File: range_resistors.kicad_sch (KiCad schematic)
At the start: 8 parts, among them U10 74HC4051

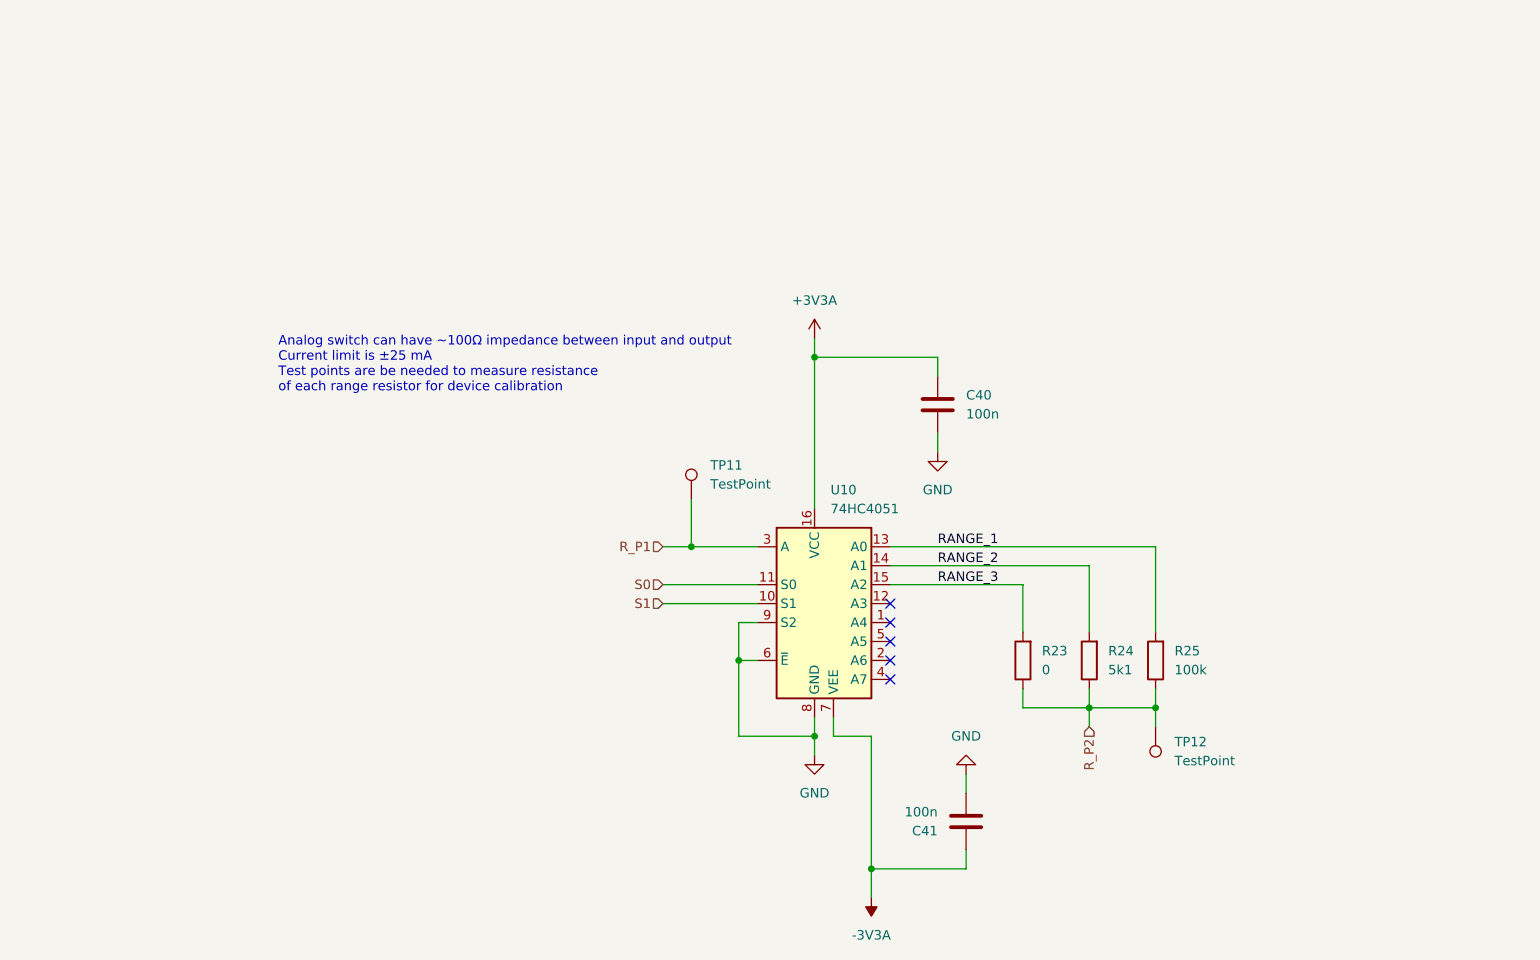
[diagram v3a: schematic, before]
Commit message: Changed range resistor selector design
Changed range resistor selector from an analog mux
to a MOSFET BPS design. This should improve on resistance, linearity,
and temperature stability for the range resistors.
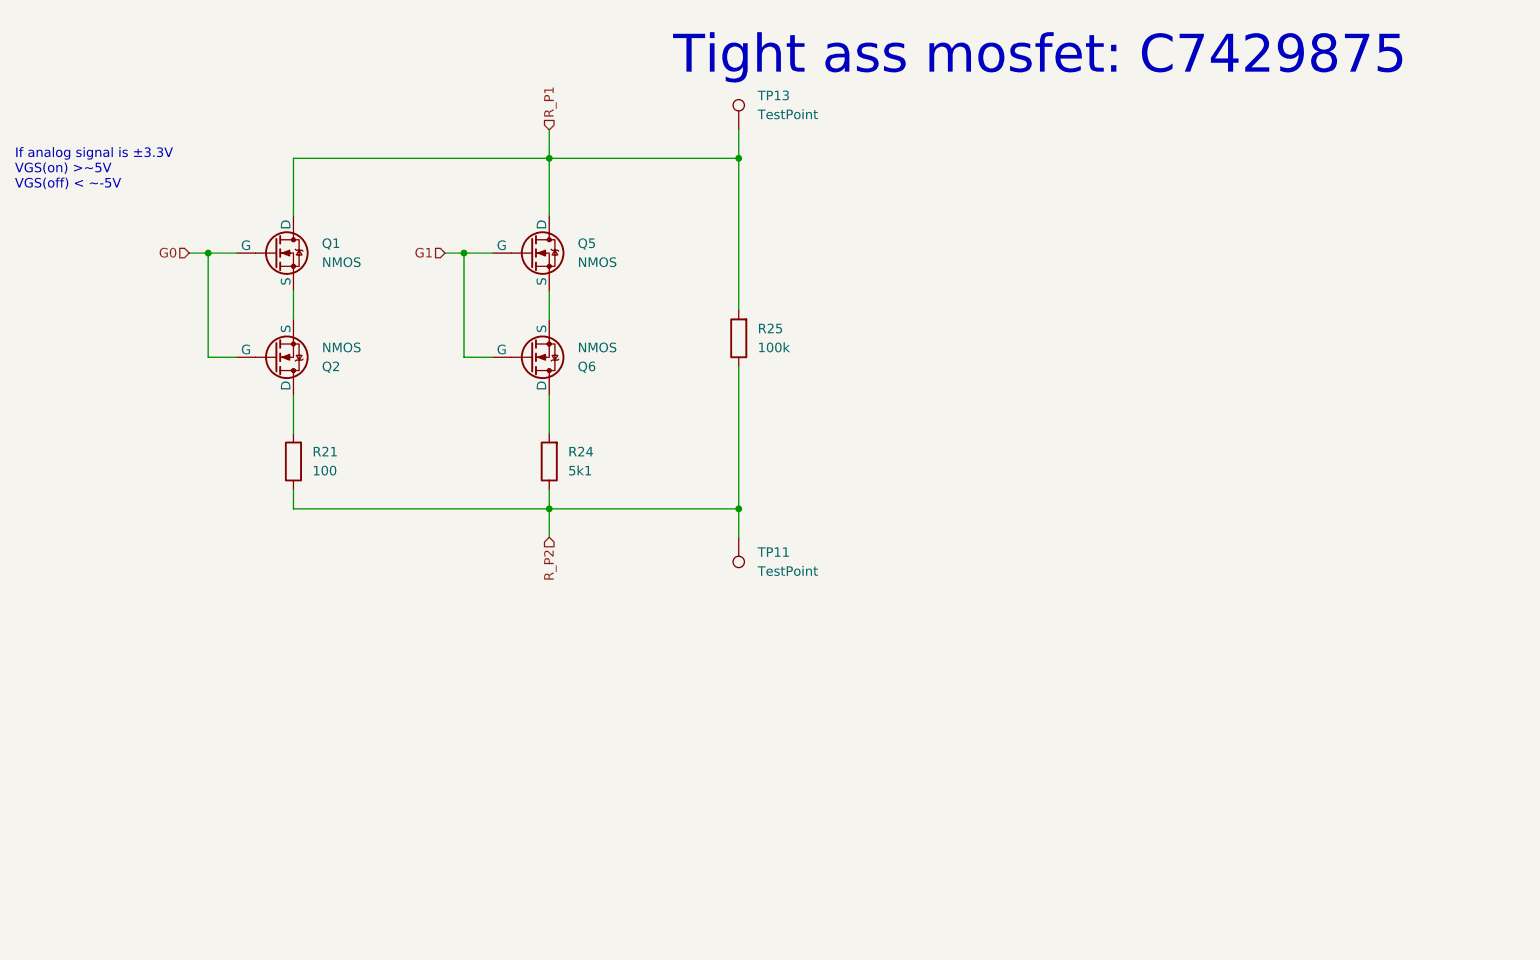
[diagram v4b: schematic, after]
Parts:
- removed C40, C41: 100n, Capacitor_SMD:C_0603_1608Metric, symbol Device:C
- removed R23: 0, Resistor_SMD:R_0603_1608Metric, symbol Device:R
- removed TP12: TestPoint, TestPoint:TestPoint_Keystone_5000-5004_Miniature, symbol Connector:TestPoint
- removed U10: 74HC4051, Package_SO:SOIC-16_3.9x9.9mm_P1.27mm, symbol 74xx:74HC4051
- added Q1, Q2, Q5, Q6: NMOS, Package_TO_SOT_SMD:SOT-23-3, symbol Simulation_SPICE:NMOS
- added R21: 100, Resistor_SMD:R_0603_1608Metric, symbol Device:R
- added TP13: TestPoint, TestPoint:TestPoint_Keystone_5000-5004_Miniature, symbol Connector:TestPoint
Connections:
- net RANGE_1 is gone; now on net R_P1: R25.2
- net R_P1: now also Q1.1 (D), Q5.1 (D), TP13.1; no longer TP11.1
- net R_P2: now also TP11.1, R21.1
- net RANGE_2: no longer names the net of R24.2
- net RANGE_2: now also Q6.1 (D)
- new net: Q2.1 (D), R21.2
- new net: Q1.3 (S), Q2.3 (S)
- new net: Q5.3 (S), Q6.3 (S)
- new net G0: Q1.2 (G), Q2.2 (G)
- new net G1: Q5.2 (G), Q6.2 (G)
- no-connect marks 5 -> 0
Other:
- note added: "If analog signal is ±3.3V VGS(on) >~5V VGS(off) < ~-5V"
- note added: "Tight ass mosfet: C7429875"
- note removed: "Analog switch can have ~100Ω impedance between input and output Current limit is ±25 mA Test points are be needed to measure resistance of each range resistor for device calibration"

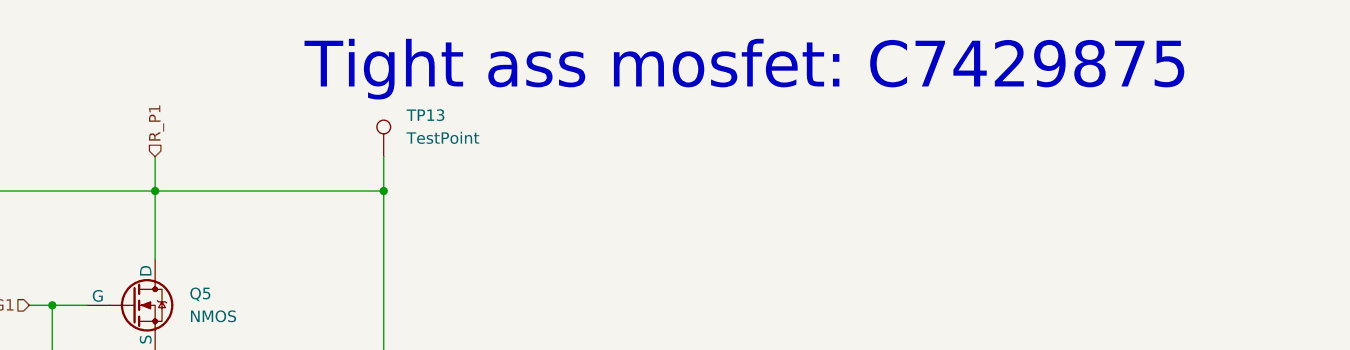
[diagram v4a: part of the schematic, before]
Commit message: Started new layout
Range resistors now use MOSFET BPS.
Currently there's no protection for over voltage on the opamp or mcu
inputs, so that needs to be done.
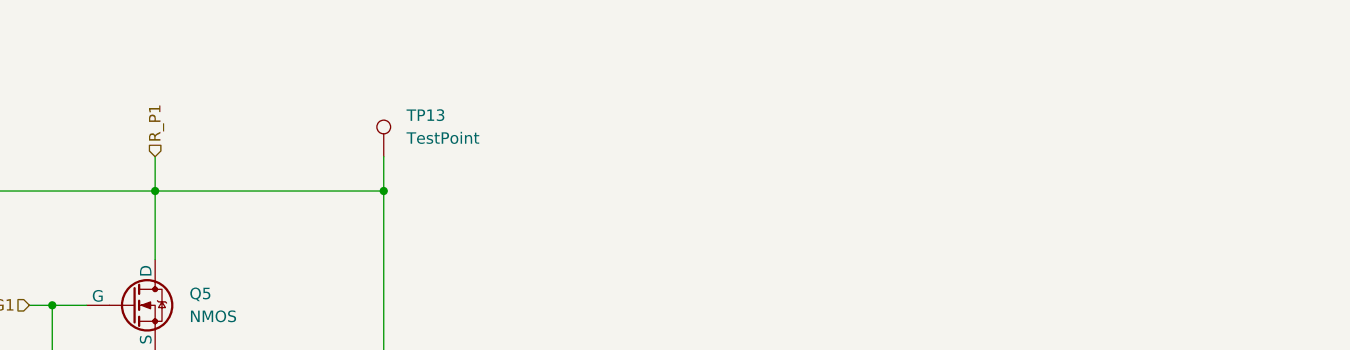
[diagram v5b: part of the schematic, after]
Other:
- note removed: "Tight ass mosfet: C7429875"
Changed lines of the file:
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@@
-		)
-	)
-	(text "Tight ass mosfet: C7429875"
-		(exclude_from_sim no)
-		(at 159.766 18.034 0)
-		(effects
-			(font
-				(size 5.08 5.08)
-			)
 		)
 	)

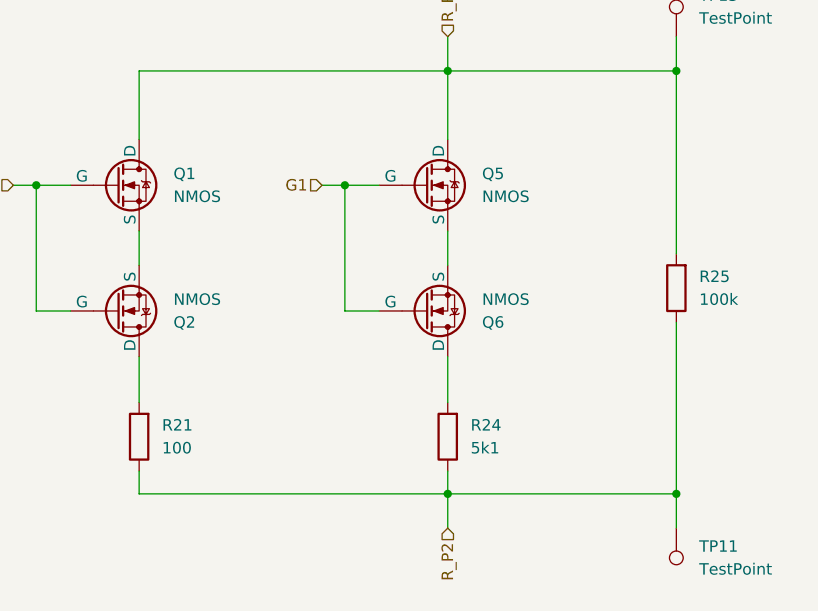
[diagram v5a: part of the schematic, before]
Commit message: Added protection to MCU analog inputs
DUT and test voltages now use clamping diodes to protect the MCU from
voltages less than 0V and greater than 3.3V.
Started laying out again, but thinking of trying something different
with the layou of the range resistors around the 1st opamp.
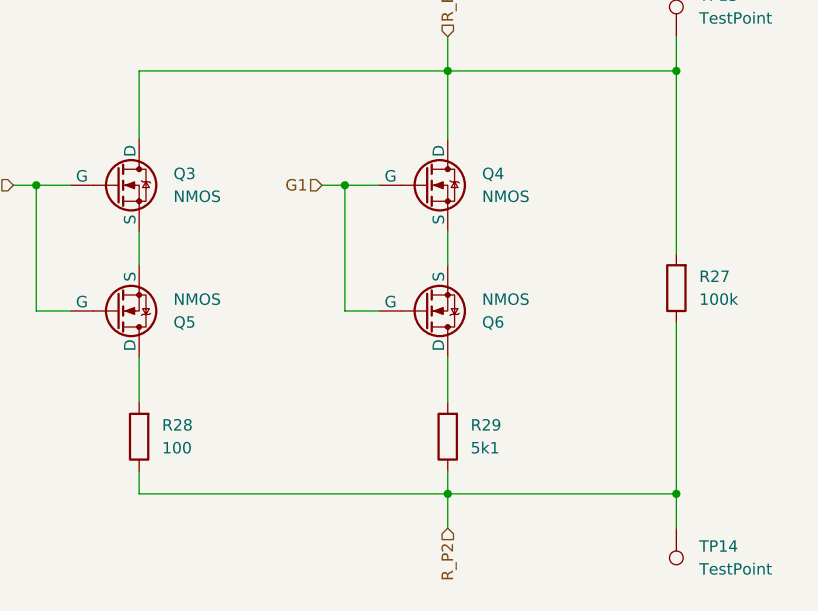
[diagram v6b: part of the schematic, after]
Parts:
- renumbered Q1 to Q3, Q5 to Q4, Q2 to Q5, R25 to R27, R21 to R28, R24 to R29, TP11 to TP14
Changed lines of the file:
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@@
 		(in_pos_files yes)
 		(dnp no)
-		(property "Reference" "Q2"
+		(property "Reference" "Q5"
 			(at 63.5 59.6901 0)
 			(show_name no)
@@
 			(project "lcr"
 				(path "/226ea51e-4da2-4daa-967e-dce167947430/c9f416db-c7a0-48f3-8fda-35fdd9af5fe5/498f4e60-134d-473a-b487-d86df052d229"
-					(reference "Q4")
+					(reference "Q9")
 					(unit 1)
 				)
 				(path "/226ea51e-4da2-4daa-967e-dce167947430/c9f416db-c7a0-48f3-8fda-35fdd9af5fe5/ec704481-2e23-475c-acd0-894f13851a8c"
-					(reference "Q2")
+					(reference "Q5")
 					(unit 1)
 				)
@@
 		(dnp no)
 		(fields_autoplaced yes)
-		(property "Reference" "R21"
+		(property "Reference" "R28"
 			(at 62.23 71.1199 0)
 			(show_name no)
@@
 			(project "lcr"
 				(path "/226ea51e-4da2-4daa-967e-dce167947430/c9f416db-c7a0-48f3-8fda-35fdd9af5fe5/498f4e60-134d-473a-b487-d86df052d229"
-					(reference "R22")
+					(reference "R31")
 					(unit 1)
 				)
 				(path "/226ea51e-4da2-4daa-967e-dce167947430/c9f416db-c7a0-48f3-8fda-35fdd9af5fe5/ec704481-2e23-475c-acd0-894f13851a8c"
-					(reference "R21")
+					(reference "R28")
 					(unit 1)
 				)
@@
 		(dnp no)
 		(fields_autoplaced yes)
-		(property "Reference" "TP11"
+		(property "Reference" "TP14"
 			(at 121.92 84.5819 0)
 			(show_name no)
@@
 			(project "lcr"
 				(path "/226ea51e-4da2-4daa-967e-dce167947430/c9f416db-c7a0-48f3-8fda-35fdd9af5fe5/498f4e60-134d-473a-b487-d86df052d229"
-					(reference "TP12")
+					(reference "TP16")
 					(unit 1)
 				)
 				(path "/226ea51e-4da2-4daa-967e-dce167947430/c9f416db-c7a0-48f3-8fda-35fdd9af5fe5/ec704481-2e23-475c-acd0-894f13851a8c"
-					(reference "TP11")
+					(reference "TP14")
 					(unit 1)
 				)
@@
 		(dnp no)
 		(fields_autoplaced yes)
-		(property "Reference" "Q5"
+		(property "Reference" "Q4"
 			(at 97.79 43.1799 0)
 			(show_name no)
@@
 			(project "lcr"
 				(path "/226ea51e-4da2-4daa-967e-dce167947430/c9f416db-c7a0-48f3-8fda-35fdd9af5fe5/498f4e60-134d-473a-b487-d86df052d229"
-					(reference "Q7")
+					(reference "Q8")
 					(unit 1)
 				)
 				(path "/226ea51e-4da2-4daa-967e-dce167947430/c9f416db-c7a0-48f3-8fda-35fdd9af5fe5/ec704481-2e23-475c-acd0-894f13851a8c"
-					(reference "Q5")
+					(reference "Q4")
 					(unit 1)
 				)
@@
 			(project "lcr"
 				(path "/226ea51e-4da2-4daa-967e-dce167947430/c9f416db-c7a0-48f3-8fda-35fdd9af5fe5/498f4e60-134d-473a-b487-d86df052d229"
-					(reference "TP14")
+					(reference "TP15")
 					(unit 1)
 				)
@@
 		(dnp no)
 		(fields_autoplaced yes)
-		(property "Reference" "R24"
+		(property "Reference" "R29"
 			(at 96.52 71.1199 0)
 			(show_name no)
@@
 			(project "lcr"
 				(path "/226ea51e-4da2-4daa-967e-dce167947430/c9f416db-c7a0-48f3-8fda-35fdd9af5fe5/498f4e60-134d-473a-b487-d86df052d229"
-					(reference "R27")
+					(reference "R32")
 					(unit 1)
 				)
 				(path "/226ea51e-4da2-4daa-967e-dce167947430/c9f416db-c7a0-48f3-8fda-35fdd9af5fe5/ec704481-2e23-475c-acd0-894f13851a8c"
-					(reference "R24")
+					(reference "R29")
 					(unit 1)
 				)
@@
 			(project "lcr"
 				(path "/226ea51e-4da2-4daa-967e-dce167947430/c9f416db-c7a0-48f3-8fda-35fdd9af5fe5/498f4e60-134d-473a-b487-d86df052d229"
-					(reference "Q8")
+					(reference "Q10")
 					(unit 1)
 				)
@@
 		(dnp no)
 		(fields_autoplaced yes)
-		(property "Reference" "Q1"
+		(property "Reference" "Q3"
 			(at 63.5 43.1799 0)
 			(show_name no)
@@
 			(project "lcr"
 				(path "/226ea51e-4da2-4daa-967e-dce167947430/c9f416db-c7a0-48f3-8fda-35fdd9af5fe5/498f4e60-134d-473a-b487-d86df052d229"
+					(reference "Q7")
+					(unit 1)
+				)
+				(path "/226ea51e-4da2-4daa-967e-dce167947430/c9f416db-c7a0-48f3-8fda-35fdd9af5fe5/ec704481-2e23-475c-acd0-894f13851a8c"
 					(reference "Q3")
-					(unit 1)
-				)
-				(path "/226ea51e-4da2-4daa-967e-dce167947430/c9f416db-c7a0-48f3-8fda-35fdd9af5fe5/ec704481-2e23-475c-acd0-894f13851a8c"
-					(reference "Q1")
 					(unit 1)
 				)
@@
 		(dnp no)
 		(fields_autoplaced yes)
-		(property "Reference" "R25"
+		(property "Reference" "R27"
 			(at 121.92 54.6099 0)
 			(show_name no)
@@
 			(project "lcr"
 				(path "/226ea51e-4da2-4daa-967e-dce167947430/c9f416db-c7a0-48f3-8fda-35fdd9af5fe5/498f4e60-134d-473a-b487-d86df052d229"
-					(reference "R28")
+					(reference "R30")
 					(unit 1)
 				)
 				(path "/226ea51e-4da2-4daa-967e-dce167947430/c9f416db-c7a0-48f3-8fda-35fdd9af5fe5/ec704481-2e23-475c-acd0-894f13851a8c"
-					(reference "R25")
-					(unit 1)
-				)
+					(reference "R27")
+					(unit 1)
+				)

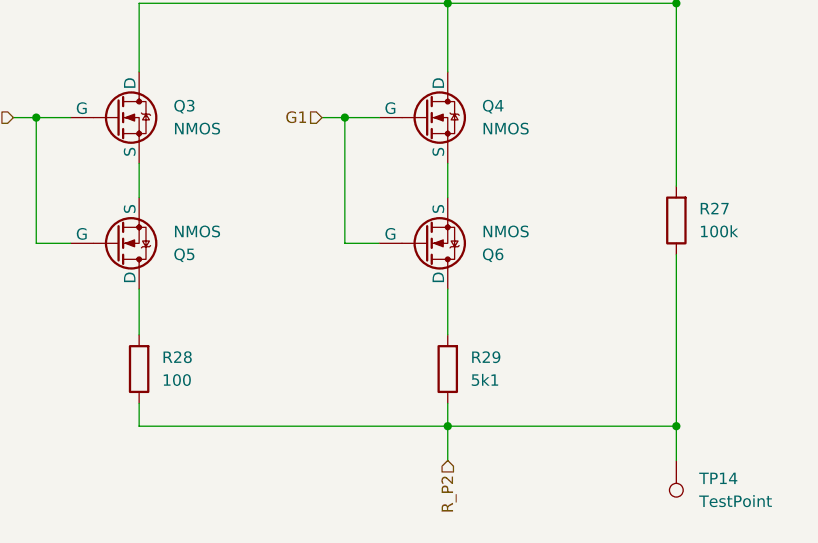
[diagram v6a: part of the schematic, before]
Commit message: Added gate drive current limiting resistors
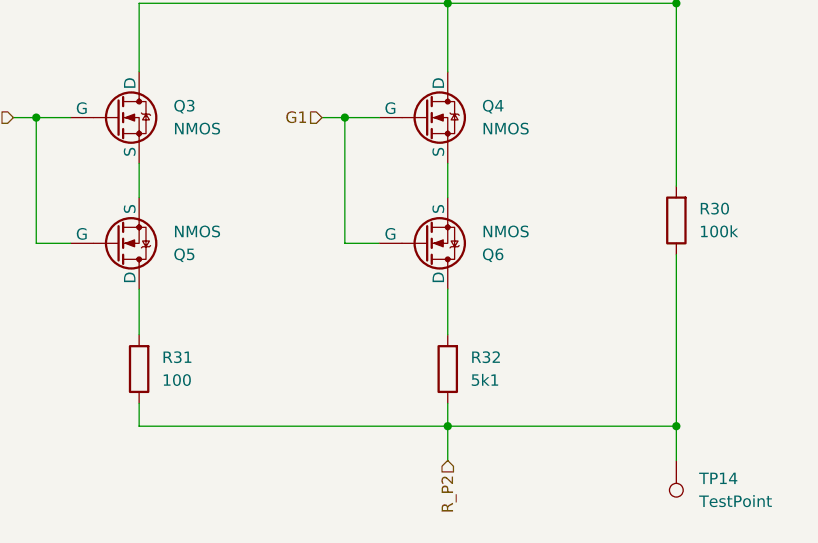
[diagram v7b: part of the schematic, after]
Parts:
- renumbered R27 to R30, R28 to R31, R29 to R32
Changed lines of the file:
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@@
 		(dnp no)
 		(fields_autoplaced yes)
-		(property "Reference" "R28"
+		(property "Reference" "R31"
 			(at 62.23 71.1199 0)
 			(show_name no)
@@
 			(project "lcr"
 				(path "/226ea51e-4da2-4daa-967e-dce167947430/c9f416db-c7a0-48f3-8fda-35fdd9af5fe5/498f4e60-134d-473a-b487-d86df052d229"
+					(reference "R34")
+					(unit 1)
+				)
+				(path "/226ea51e-4da2-4daa-967e-dce167947430/c9f416db-c7a0-48f3-8fda-35fdd9af5fe5/ec704481-2e23-475c-acd0-894f13851a8c"
 					(reference "R31")
-					(unit 1)
-				)
-				(path "/226ea51e-4da2-4daa-967e-dce167947430/c9f416db-c7a0-48f3-8fda-35fdd9af5fe5/ec704481-2e23-475c-acd0-894f13851a8c"
-					(reference "R28")
 					(unit 1)
 				)
@@
 		(dnp no)
 		(fields_autoplaced yes)
-		(property "Reference" "R29"
+		(property "Reference" "R32"
 			(at 96.52 71.1199 0)
 			(show_name no)
@@
 			(project "lcr"
 				(path "/226ea51e-4da2-4daa-967e-dce167947430/c9f416db-c7a0-48f3-8fda-35fdd9af5fe5/498f4e60-134d-473a-b487-d86df052d229"
+					(reference "R35")
+					(unit 1)
+				)
+				(path "/226ea51e-4da2-4daa-967e-dce167947430/c9f416db-c7a0-48f3-8fda-35fdd9af5fe5/ec704481-2e23-475c-acd0-894f13851a8c"
 					(reference "R32")
-					(unit 1)
-				)
-				(path "/226ea51e-4da2-4daa-967e-dce167947430/c9f416db-c7a0-48f3-8fda-35fdd9af5fe5/ec704481-2e23-475c-acd0-894f13851a8c"
-					(reference "R29")
 					(unit 1)
 				)
@@
 		(dnp no)
 		(fields_autoplaced yes)
-		(property "Reference" "R27"
+		(property "Reference" "R30"
 			(at 121.92 54.6099 0)
 			(show_name no)
@@
 			(project "lcr"
 				(path "/226ea51e-4da2-4daa-967e-dce167947430/c9f416db-c7a0-48f3-8fda-35fdd9af5fe5/498f4e60-134d-473a-b487-d86df052d229"
+					(reference "R33")
+					(unit 1)
+				)
+				(path "/226ea51e-4da2-4daa-967e-dce167947430/c9f416db-c7a0-48f3-8fda-35fdd9af5fe5/ec704481-2e23-475c-acd0-894f13851a8c"
 					(reference "R30")
 					(unit 1)
 				)
-				(path "/226ea51e-4da2-4daa-967e-dce167947430/c9f416db-c7a0-48f3-8fda-35fdd9af5fe5/ec704481-2e23-475c-acd0-894f13851a8c"
-					(reference "R27")
-					(unit 1)
-				)
